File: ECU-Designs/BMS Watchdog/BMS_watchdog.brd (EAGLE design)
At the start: 18.2 x 25.4 mm, 4 parts, among them X1 MINIFIT_5566-4

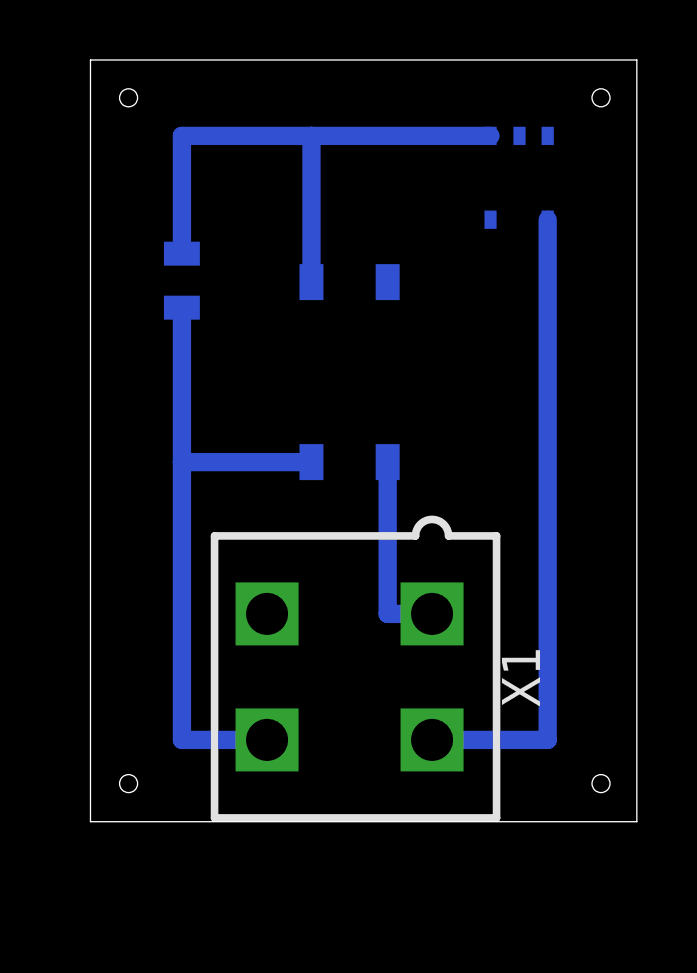
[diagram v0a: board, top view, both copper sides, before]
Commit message: Updated BMS watchdog
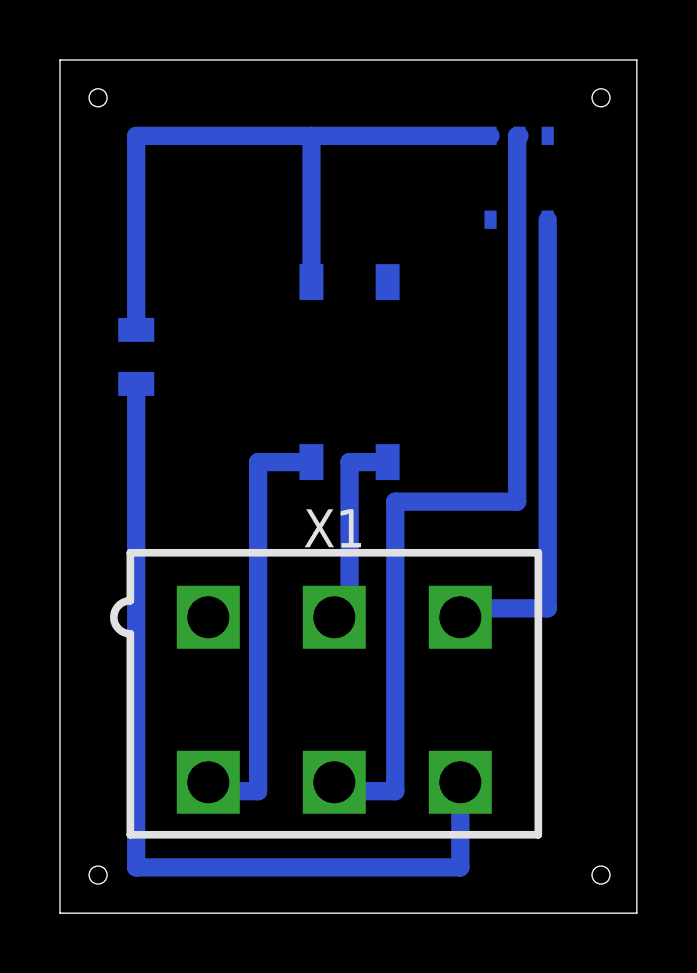
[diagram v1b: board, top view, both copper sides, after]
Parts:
- R1: value (none) -> 210
- X1: value MINIFIT_5566-4 -> MINIFIT_5566-6; device HyTechDevices:MINIFIT_5566-4 -> HyTechDevices:MINIFIT_5566-6
- moved R1 2.96 mm to (74.2, 24.6)
- moved X1 0.92 mm to (80.8, 13.2), turned to 180 degrees
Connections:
- new net GND: U$1.GND, X1.5
- new net N$4: U$2.4, X1.4
- net N$1: now also X1.6; no longer U$2.4, X1.4
- net N$2: now also X1.3; no longer X1.2
- net N$5: now also X1.2; no longer X1.1
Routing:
- net GND: track 0.00 -> 28.3 mm
- net N$4: track 0.00 -> 14.7 mm
- net N$1: track 21.6 -> 29.8 mm
- net N$2: track 21.2 -> 16.2 mm
- net N$3: track 19.1 -> 23.2 mm
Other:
- board size 18.2 x 25.4 mm -> 19.2 x 28.4 mm
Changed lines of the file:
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@@
 <board>
 <plain>
-<wire x1="72.644" y1="9.144" x2="90.856" y2="9.144" width="0" layer="20"/>
-<wire x1="90.856" y1="9.144" x2="90.856" y2="34.534" width="0" layer="20"/>
-<wire x1="90.856" y1="34.534" x2="72.644" y2="34.534" width="0" layer="20"/>
-<wire x1="72.644" y1="34.534" x2="72.644" y2="9.144" width="0" layer="20"/>
-<hole x="73.914" y="33.274" drill="0.6"/>
+<wire x1="71.628" y1="6.096" x2="90.856" y2="6.096" width="0" layer="20"/>
+<wire x1="90.856" y1="6.096" x2="90.856" y2="34.534" width="0" layer="20"/>
+<wire x1="90.856" y1="34.534" x2="71.628" y2="34.534" width="0" layer="20"/>
+<wire x1="71.628" y1="34.534" x2="71.628" y2="6.096" width="0" layer="20"/>
+<hole x="72.898" y="33.274" drill="0.6"/>
 <hole x="89.662" y="33.274" drill="0.6"/>
-<hole x="89.662" y="10.414" drill="0.6"/>
-<hole x="73.914" y="10.414" drill="0.6"/>
+<hole x="89.662" y="7.366" drill="0.6"/>
+<hole x="72.898" y="7.366" drill="0.6"/>
 </plain>
 <attributes>
@@
 </autorouter>
 <elements>
-<element name="R1" library="HyTechDevices" package="0805" value="" x="75.692" y="27.178" rot="MR270"/>
+<element name="R1" library="HyTechDevices" package="0805" value="210" x="74.168" y="24.638" rot="MR270"/>
 <element name="U$1" library="HyTechDevices" package="SOT23-5" value="STWD100" x="87.884" y="29.21" rot="MR270"/>
 <element name="U$2" library="HyTechDevices" package="SOP04" value="CPC1002N" x="81.28" y="24.13" rot="MR180"/>
-<element name="X1" library="HyTechDevices" package="MINIFIT_5566-4" value="MINIFIT_5566-4" x="81.28" y="13.97" rot="R90">
-<attribute name="OC_NEWARK" value="unknown" x="81.28" y="13.97" size="1.778" layer="27" rot="R90" display="off"/>
-<attribute name="OC_FARNELL" value="unknown" x="81.28" y="13.97" size="1.778" layer="27" rot="R90" display="off"/>
-<attribute name="MF" value="" x="81.28" y="13.97" size="1.778" layer="27" rot="R90" display="off"/>
-<attribute name="MPN" value="" x="81.28" y="13.97" size="1.778" layer="27" rot="R90" display="off"/>
+<element name="X1" library="HyTechDevices" package="MINIFIT_5566-6" value="MINIFIT_5566-6" x="80.772" y="13.208" rot="R180">
+<attribute name="OC_NEWARK" value="22K8620" x="80.772" y="13.208" size="1.778" layer="27" rot="R180" display="off"/>
+<attribute name="OC_FARNELL" value="unknown" x="80.772" y="13.208" size="1.778" layer="27" rot="R180" display="off"/>
+<attribute name="MF" value="" x="80.772" y="13.208" size="1.778" layer="27" rot="R180" display="off"/>
+<attribute name="MPN" value="95566-61002" x="80.772" y="13.208" size="1.778" layer="27" rot="R180" display="off"/>
 </element>
 </elements>
@@
 <contactref element="R1" pad="1"/>
 <contactref element="U$2" pad="1"/>
-<wire x1="75.692" y1="28.078" x2="75.692" y2="32.004" width="0.6096" layer="16"/>
-<wire x1="75.692" y1="32.004" x2="80.01" y2="32.004" width="0.6096" layer="16"/>
+<wire x1="74.168" y1="25.538" x2="74.168" y2="32.004" width="0.6096" layer="16"/>
+<wire x1="74.168" y1="32.004" x2="80.01" y2="32.004" width="0.6096" layer="16"/>
 <wire x1="80.01" y1="32.004" x2="85.979" y2="32.004" width="0.6096" layer="16"/>
 <wire x1="80.01" y1="27.13" x2="80.01" y2="32.004" width="0.6096" layer="16"/>
@@
 <signal name="N$2">
 <contactref element="U$1" pad="WDI"/>
-<contactref element="X1" pad="2"/>
-<wire x1="84.03" y1="11.87" x2="87.884" y2="11.87" width="0.6096" layer="16"/>
-<wire x1="87.884" y1="11.87" x2="87.884" y2="29.21" width="0.6096" layer="16"/>
+<contactref element="X1" pad="3"/>
+<wire x1="87.884" y1="29.21" x2="87.884" y2="16.256" width="0.6096" layer="16"/>
+<wire x1="87.884" y1="16.256" x2="84.972" y2="16.256" width="0.6096" layer="16"/>
+<wire x1="84.972" y1="16.256" x2="84.972" y2="15.958" width="0.6096" layer="16"/>
 </signal>
 <signal name="N$1">
-<contactref element="X1" pad="4"/>
 <contactref element="R1" pad="2"/>
-<contactref element="U$2" pad="4"/>
-<wire x1="75.692" y1="21.13" x2="75.692" y2="11.87" width="0.6096" layer="16"/>
-<wire x1="75.692" y1="11.87" x2="78.53" y2="11.87" width="0.6096" layer="16"/>
-<wire x1="75.692" y1="26.278" x2="75.692" y2="21.13" width="0.6096" layer="16"/>
-<wire x1="75.692" y1="21.13" x2="80.01" y2="21.13" width="0.6096" layer="16"/>
+<wire x1="74.168" y1="23.738" x2="74.168" y2="7.62" width="0.6096" layer="16"/>
+<contactref element="X1" pad="6"/>
+<wire x1="74.168" y1="7.62" x2="84.972" y2="7.62" width="0.6096" layer="16"/>
+<wire x1="84.972" y1="7.62" x2="84.972" y2="10.458" width="0.6096" layer="16"/>
 </signal>
 <signal name="N$5">
 <contactref element="U$2" pad="3"/>
-<contactref element="X1" pad="1"/>
-<wire x1="82.55" y1="21.13" x2="82.55" y2="16.07" width="0.6096" layer="16"/>
-<wire x1="82.55" y1="16.07" x2="84.03" y2="16.07" width="0.6096" layer="16"/>
+<contactref element="X1" pad="2"/>
+<wire x1="82.55" y1="21.13" x2="81.28" y2="21.13" width="0.6096" layer="16"/>
+<wire x1="81.28" y1="21.13" x2="81.28" y2="16.256" width="0.6096" layer="16"/>
+<wire x1="81.28" y1="16.256" x2="80.772" y2="16.256" width="0.6096" layer="16"/>
+<wire x1="80.772" y1="16.256" x2="80.772" y2="15.958" width="0.6096" layer="16"/>
 </signal>
 <signal name="N$6">
@@
 </signal>
 <signal name="GND">
+<contactref element="X1" pad="5"/>
+<contactref element="U$1" pad="GND"/>
+<wire x1="86.9442" y1="32.004" x2="86.868" y2="32.004" width="0.6096" layer="16"/>
+<wire x1="86.868" y1="32.004" x2="86.868" y2="19.812" width="0.6096" layer="16"/>
+<wire x1="86.868" y1="19.812" x2="82.804" y2="19.812" width="0.6096" layer="16"/>
+<wire x1="82.804" y1="19.812" x2="82.804" y2="10.16" width="0.6096" layer="16"/>
+<wire x1="82.804" y1="10.16" x2="80.772" y2="10.16" width="0.6096" layer="16"/>
+<wire x1="80.772" y1="10.16" x2="80.772" y2="10.458" width="0.6096" layer="16"/>
+</signal>
+<signal name="N$4">
+<contactref element="U$2" pad="4"/>
+<contactref element="X1" pad="4"/>
+<wire x1="80.01" y1="21.13" x2="78.232" y2="21.13" width="0.6096" layer="16"/>
+<wire x1="78.232" y1="21.13" x2="78.232" y2="10.16" width="0.6096" layer="16"/>
+<wire x1="78.232" y1="10.16" x2="76.572" y2="10.16" width="0.6096" layer="16"/>
+<wire x1="76.572" y1="10.16" x2="76.572" y2="10.458" width="0.6096" layer="16"/>
 </signal>
 </signals>
